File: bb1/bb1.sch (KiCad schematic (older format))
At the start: 48 parts, among them CON1 SD_Card, P1 CONN_01X02, P10 CONN_01X02, P12 CONN_01X02, P2 CONN_01X02, P3 CONN_01X02, P4 CONN_01X02, P5 CONN_01X02, P6 CONN_02X02, P7 CONN_01X02, P8 CONN_02X04, P9 CONN_02X02, Q1 MMBT3904, SW1 SW_PUSH, U1 ESP-13-WROOM-02, U2 MCP2551-I/SN, U3 WS2812RGB, U4 SN75C3222E, U5 ILI9341_LCD_Breakout, U6 WS2812RGB, U7 WS2812RGB, U8 Teensy_3.1, U9 TL2575

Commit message: v0.1 almost done now. Schematic + Board
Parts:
- removed C1, C6, C8: C_Small, Capacitors_SMD:C_1206_HandSoldering, symbol C_Small
- removed C2, C4, C5, C7: .1uF, Capacitors_SMD:C_1206_HandSoldering, symbol C_Small
- removed D1, D3: ZENERsmall, Diodes_SMD:SOD-323, symbol ZENERsmall
- removed F1: FUSE, Fuse_Holders_and_Fuses:Fuseholder5x20_horiz_SemiClosed_Casing10x25mm, symbol FUSE
- removed P1, P10, P12, P2, P3, P4, P5, P7: CONN_01X02, Terminal_Blocks:TerminalBlock_Pheonix_PT-3.5mm_2pol, symbol CONN_01X02
- removed P6, P9: CONN_02X02, Pin_Headers:Pin_Header_Straight_2x02, symbol CONN_02X02
- removed R3: 10k, Resistors_SMD:R_1206_HandSoldering, symbol R
- removed R4, R9: 68k, Resistors_SMD:R_1206_HandSoldering, symbol R
- removed SW1: SW_PUSH, Buttons_Switches_SMD:SW_SPST_FSMSM, symbol SW_PUSH
- removed U2: MCP2551-I/SN, Power_Integrations:SO-8, symbol MCP2551-I/SN
- removed U3, U6, U7: WS2812RGB, symbol WS2812RGB
- removed U4: SN75C3222E, SMD_Packages:SSOP-20, symbol SN75C3222E
- removed U8: Teensy_3.1, kicad-teensy31:Teensy-3.1, symbol Teensy_3.1
- added C24, C25, C27, C28: .1uF, Capacitors_SMD:C_0603_HandSoldering, symbol C_Small
- added E1: Encoder_switch, w_misc_comp:encoder_alps-ec12d, symbol Encoder_switch
- added P10: SPI_DBG, bb:HEADER_2x4_0.05, symbol CONN_02X04
- added P11: RX1, Measurement_Points:Measurement_Point_Round-TH_Small, symbol CONN_01X01
- added P12: RX2, Measurement_Points:Measurement_Point_Round-TH_Small, symbol CONN_01X01
- added P13: CAN_RX, Measurement_Points:Measurement_Point_Round-TH_Small, symbol CONN_01X01
- added P14: CAN_TX, Measurement_Points:Measurement_Point_Round-TH_Small, symbol CONN_01X01
- added P3: CONN_01X08, Pin_Headers:Pin_Header_Straight_1x08, symbol CONN_01X08
- added R21, R22: 4.7k, Resistors_SMD:R_0603_HandSoldering, symbol R
- added R6: 10k, Resistors_SMD:R_0603_HandSoldering, symbol R
- added R7: 56k .1%, Resistors_SMD:R_0603_HandSoldering, symbol R
- added SW3: SW_PUSH, bb:SWITCH_SMD_3x6, symbol SW_PUSH
- added U13: BMP280, bb:BMP280, symbol BMP280
- added U14: MPL3115A2, bb:MPL3115A2, symbol MPL3115A2
- added U2: WIFI_RGB, bb:WS2818RGB, symbol WS2812RGB
- added U4: N2K_RGB, bb:WS2818RGB, symbol WS2812RGB
- added U5: NMEA_RGB, bb:WS2818RGB, symbol WS2812RGB
- C1: renamed from C9; footprint Capacitors_SMD:c_elec_6.3x5.3 -> Capacitors_ThroughHole:C_Radial_D8_L11.5_P3.5
- C2: renamed from C10; footprint Capacitors_SMD:c_elec_6.3x5.3 -> Capacitors_ThroughHole:C_Radial_D6.3_L11.2_P2.5
- C3: value 0.1uF -> .1uF; footprint Capacitors_SMD:C_1206_HandSoldering -> Capacitors_SMD:C_0603_HandSoldering
- CON1: footprint 10067847-001 -> w_conn_misc:microsd_socket
- D1: renamed from D4; footprint Diodes_SMD:SOD-323 -> Diodes_SMD:SOD-123
- D2: value ZENERsmall -> 5.1V
- L1: footprint Inductors:SELF-WE-TPC_M -> bb:SRN1060_HANDSOLDER
- P2: renamed from P8; value CONN_02X04 -> WIFI_DBG; footprint Pin_Headers:Pin_Header_Straight_2x04 -> bb:HEADER_2x4_0.05
- R1: footprint Resistors_SMD:R_1206_HandSoldering -> Resistors_SMD:R_0603_HandSoldering
- R2: value 68k -> 10k; footprint Resistors_SMD:R_1206_HandSoldering -> Resistors_SMD:R_0603_HandSoldering
- R3: renamed from R5; footprint Resistors_SMD:R_1206_HandSoldering -> Resistors_SMD:R_0603_HandSoldering
- R4: renamed from R6; footprint Resistors_SMD:R_1206_HandSoldering -> Resistors_SMD:R_0603_HandSoldering
- R5: renamed from R7; footprint Resistors_SMD:R_1206_HandSoldering -> Resistors_SMD:R_0603_HandSoldering
- R8: value 10k -> 10k .1%; footprint Resistors_SMD:R_1206_HandSoldering -> Resistors_SMD:R_0603_HandSoldering
- U6: renamed from U5; footprint (none) -> bb:ILI9341
- renumbered U9 to U1, U1 to U3
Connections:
- net labels added: CAN_STBY, SCL1, SDA1, SER_EN
- net labels removed: AUX1, AUX2, CAN_RX, CAN_TX, N2K_H, N2K_L, NMEA1_RX, NMEA1_TX, NMEA2_RX, NMEA2_TX, SER1_RX, SER1_TX, SER2_RX, SER2_TX
- wire segments 215 -> 221
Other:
- moved on the sheet: C1, C2, D1, L1, Q1, R3, R4, R5, U1, U6

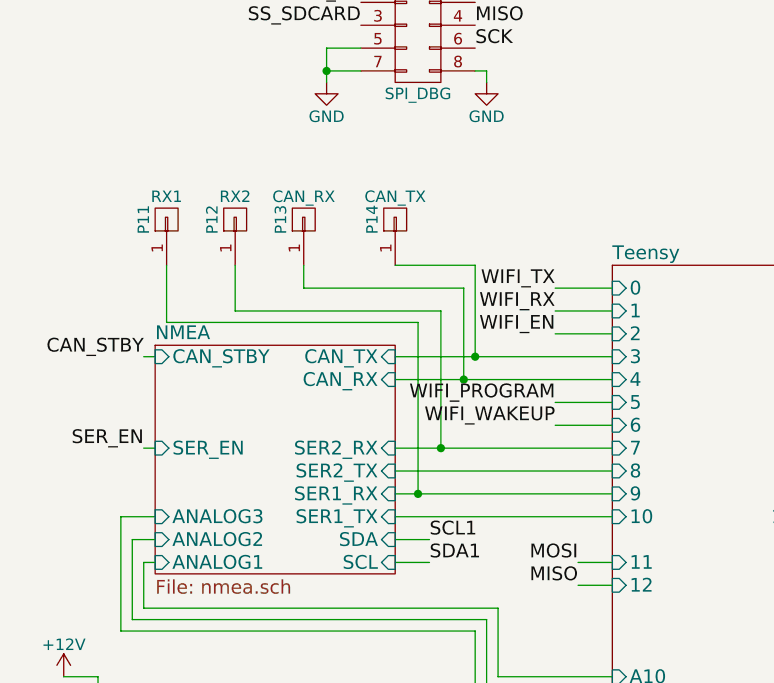
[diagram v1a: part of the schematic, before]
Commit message: Fine tuning of the board
- Added test headers for serial1, serial2 and can (at 3.3v levels)
- Added solder jumpers to disconnect serial2 from rs232 converter
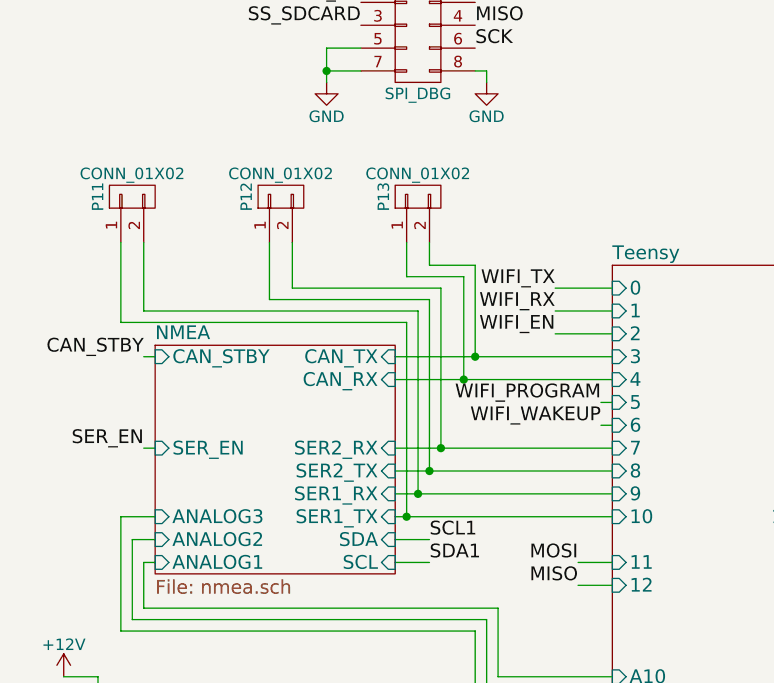
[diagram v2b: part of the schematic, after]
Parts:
- removed P11: RX1, Measurement_Points:Measurement_Point_Round-TH_Small, symbol CONN_01X01
- removed P12: RX2, Measurement_Points:Measurement_Point_Round-TH_Small, symbol CONN_01X01
- removed P13: CAN_RX, Measurement_Points:Measurement_Point_Round-TH_Small, symbol CONN_01X01
- removed P14: CAN_TX, Measurement_Points:Measurement_Point_Round-TH_Small, symbol CONN_01X01
- added P11, P12, P13: CONN_01X02, Pin_Headers:Pin_Header_Straight_1x02, symbol CONN_01X02
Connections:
- net NMEA/CAN_RX: now also P13.1 (P1)
- net NMEA/CAN_TX: now also P13.2 (P2)
- net NMEA/SER1_RX: now also P11.2 (P2)
- net NMEA/SER1_TX: now also P11.1 (P1)
- net NMEA/SER2_RX: now also P12.2 (P2)
- net NMEA/SER2_TX: now also P12.1 (P1)
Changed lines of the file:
@@
 F14 "SCL" I R 2150 5700 60
 $EndSheet
-Text Label 2850 5000 2    60   ~ 0
+Text Label 3050 5000 2    60   ~ 0
 WIFI_PROGRAM
-Text Label 2850 5100 2    60   ~ 0
+Text Label 3050 5100 2    60   ~ 0
 WIFI_WAKEUP
 Text Label 2950 5700 2    60   ~ 0
@@
 	2150 4900 3100 4900
 Wire Wire Line
-	2850 5000 3100 5000
-Wire Wire Line
-	3100 5100 2850 5100
+	3050 5000 3100 5000
+Wire Wire Line
+	3100 5100 3050 5100
 Wire Wire Line
 	2150 5500 3100 5500
@@
 Wire Wire Line
 	2550 3550 2550 3600
-$Comp
-L CONN_01X01 P13
-U 1 1 56665450
-P 1750 4200
-F 0 "P13" H 1750 4300 50  0000 C CNN
-F 1 "CAN_RX" V 1850 4200 50  0000 C CNN
-F 2 "Measurement_Points:Measurement_Point_Round-TH_Small" H 1750 4200 60  0001 C CNN
-F 3 "" H 1750 4200 60  0000 C CNN
-	1    1750 4200
-	0    -1   -1   0
-$EndComp
-$Comp
-L CONN_01X01 P14
-U 1 1 56666F3A
-P 2150 4200
-F 0 "P14" H 2150 4300 50  0000 C CNN
-F 1 "CAN_TX" V 2250 4200 50  0000 C CNN
-F 2 "Measurement_Points:Measurement_Point_Round-TH_Small" H 2150 4200 60  0001 C CNN
-F 3 "" H 2150 4200 60  0000 C CNN
-	1    2150 4200
-	0    -1   -1   0
-$EndComp
-Wire Wire Line
-	2500 4800 2500 4400
-Wire Wire Line
-	2500 4400 2150 4400
+Wire Wire Line
+	2500 4400 2500 4800
 Connection ~ 2500 4800
 Wire Wire Line
-	2450 4900 2450 4500
-Wire Wire Line
-	2450 4500 1750 4500
-Wire Wire Line
-	1750 4500 1750 4400
+	2450 4900 2450 4450
+Wire Wire Line
+	2450 4450 2200 4450
+Wire Wire Line
+	2200 4450 2200 4300
 Connection ~ 2450 4900
-$Comp
-L CONN_01X01 P12
-U 1 1 56675FE9
-P 1450 4200
-F 0 "P12" H 1450 4300 50  0000 C CNN
-F 1 "RX2" V 1550 4200 50  0000 C CNN
-F 2 "Measurement_Points:Measurement_Point_Round-TH_Small" H 1450 4200 60  0001 C CNN
-F 3 "" H 1450 4200 60  0000 C CNN
-	1    1450 4200
-	0    -1   -1   0
-$EndComp
-$Comp
-L CONN_01X01 P11
-U 1 1 566761A9
-P 1150 4200
-F 0 "P11" H 1150 4300 50  0000 C CNN
-F 1 "RX1" V 1250 4200 50  0000 C CNN
-F 2 "Measurement_Points:Measurement_Point_Round-TH_Small" H 1150 4200 60  0001 C CNN
-F 3 "" H 1150 4200 60  0000 C CNN
-	1    1150 4200
-	0    -1   -1   0
-$EndComp
-Wire Wire Line
-	1450 4400 1450 4600
-Wire Wire Line
-	1450 4600 2350 4600
-Wire Wire Line
-	2350 4600 2350 5200
+Wire Wire Line
+	1700 4300 1700 4500
+Wire Wire Line
+	1700 4500 2350 4500
+Wire Wire Line
+	2350 4500 2350 5200
 Connection ~ 2350 5200
 Wire Wire Line
-	1150 4400 1150 4650
-Wire Wire Line
-	1150 4650 2250 4650
-Wire Wire Line
-	2250 4650 2250 5400
+	1050 4300 1050 4600
+Wire Wire Line
+	1050 4600 2250 4600
+Wire Wire Line
+	2250 4600 2250 5400
 Connection ~ 2250 5400
 Wire Wire Line
@@
 SDA1
 NoConn ~ 3100 6500
+Wire Wire Line
+	1600 4300 1600 4550
+Wire Wire Line
+	1600 4550 2300 4550
+Wire Wire Line
+	2300 4550 2300 5300
+Connection ~ 2300 5300
+Wire Wire Line
+	2200 5500 2200 4650
+Wire Wire Line
+	2200 4650 950  4650
+Wire Wire Line
+	950  4650 950  4300
+Connection ~ 2200 5500
+$Comp
+L CONN_01X02 P11
+U 1 1 56608870
+P 1000 4100
+F 0 "P11" H 1000 4250 50  0000 C CNN
+F 1 "CONN_01X02" V 1100 4100 50  0000 C CNN
+F 2 "Pin_Headers:Pin_Header_Straight_1x02" H 1000 4100 60  0001 C CNN
+F 3 "" H 1000 4100 60  0000 C CNN
+	1    1000 4100
+	0    -1   -1   0
+$EndComp
+$Comp
+L CONN_01X02 P12
+U 1 1 56608D47
+P 1650 4100
+F 0 "P12" H 1650 4250 50  0000 C CNN
+F 1 "CONN_01X02" V 1750 4100 50  0000 C CNN
+F 2 "Pin_Headers:Pin_Header_Straight_1x02" H 1650 4100 60  0001 C CNN
+F 3 "" H 1650 4100 60  0000 C CNN
+	1    1650 4100
+	0    -1   -1   0
+$EndComp
+$Comp
+L CONN_01X02 P13
+U 1 1 5660A2E6
+P 2250 4100
+F 0 "P13" H 2250 4250 50  0000 C CNN
+F 1 "CONN_01X02" V 2350 4100 50  0000 C CNN
+F 2 "Pin_Headers:Pin_Header_Straight_1x02" H 2250 4100 60  0001 C CNN
+F 3 "" H 2250 4100 60  0000 C CNN
+	1    2250 4100
+	0    -1   -1   0
+$EndComp
+Wire Wire Line
+	2500 4400 2300 4400
+Wire Wire Line
+	2300 4400 2300 4300
 $EndSCHEMATC

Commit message: Continued work on the PCB. Lots of footprint work.
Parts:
- removed CON1: SD_Card, w_conn_misc:microsd_socket, symbol SD_Card
- added CON1: MICROSD, bb:DM3CS-SF, symbol MICROSD
- U1: value TL2575 -> U1
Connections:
- net +3V3: now also P3.8 (P8), CON1.4 (Vdd); no longer P3.1 (P1)
- net GND: now also P3.1 (P1), CON1.6 (VSS); no longer P3.8 (P8)
- net MISO: now also CON1.7 (DAT0/DO)
- net MOSI: now also CON1.3 (CMD/DI)
- net SCK: now also CON1.5 (CLK/SCLK)
- net SS_SDCARD: now also CON1.2 (DAT3/CS)

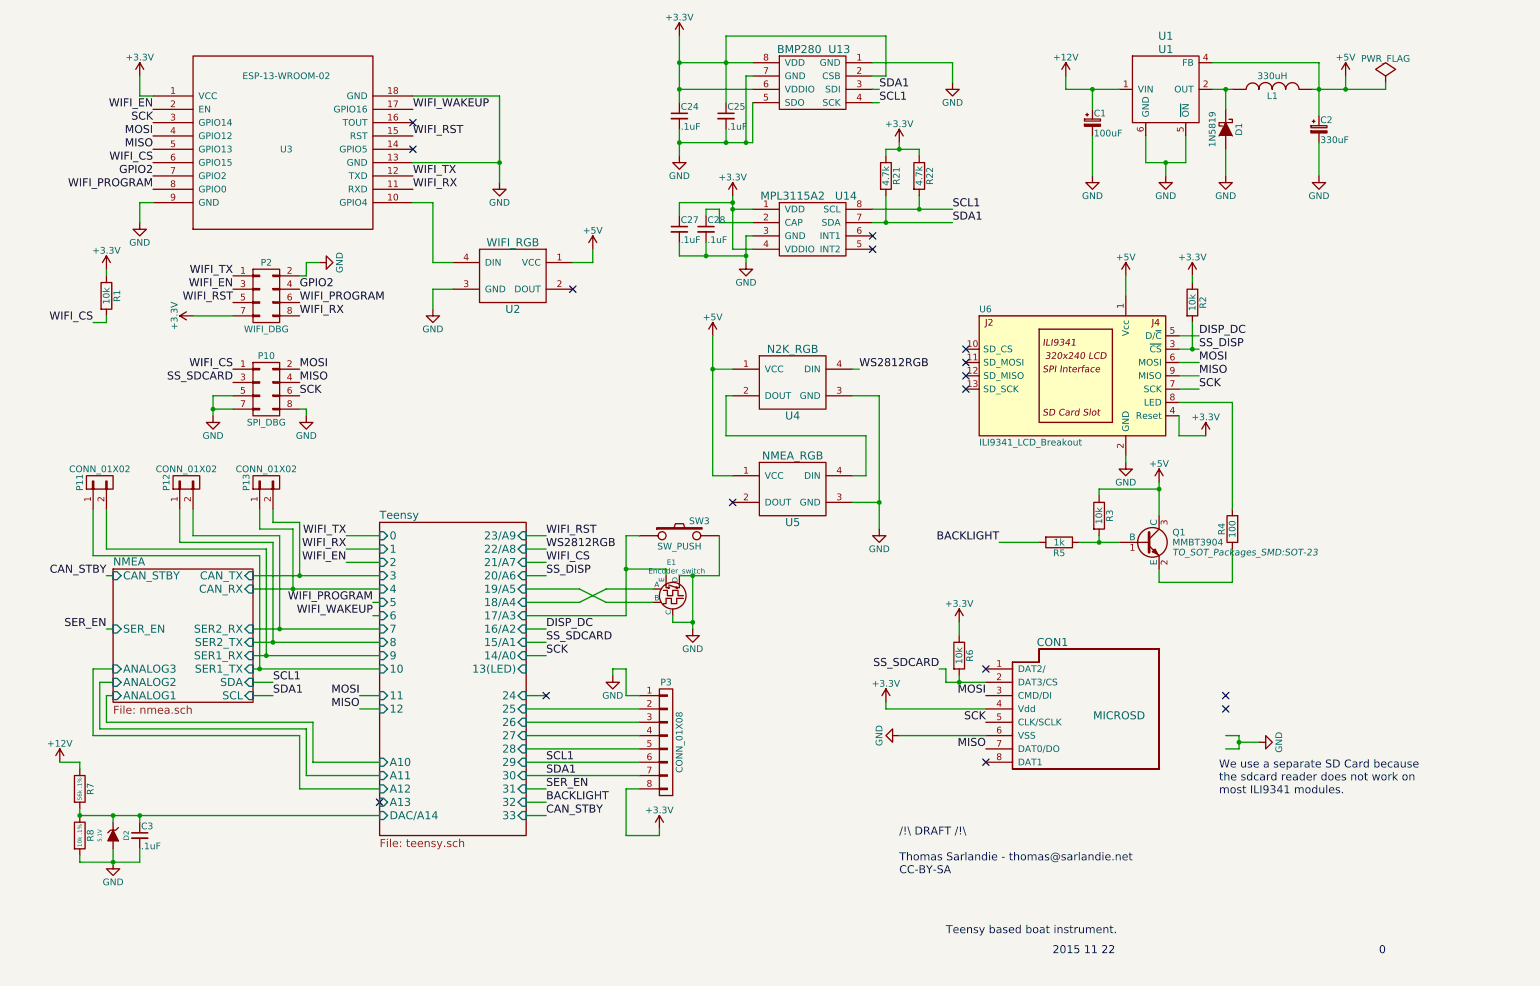
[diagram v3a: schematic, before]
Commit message: Finalized v1 revA
 - Added BNO055
 - Fixed SOIC8 pattern
 - Replaced phoenix connectors by a 20 pol
 - Many fine tuning/cosmetic adjustments
 - Sent files to manufacturing. Will tag this commit.
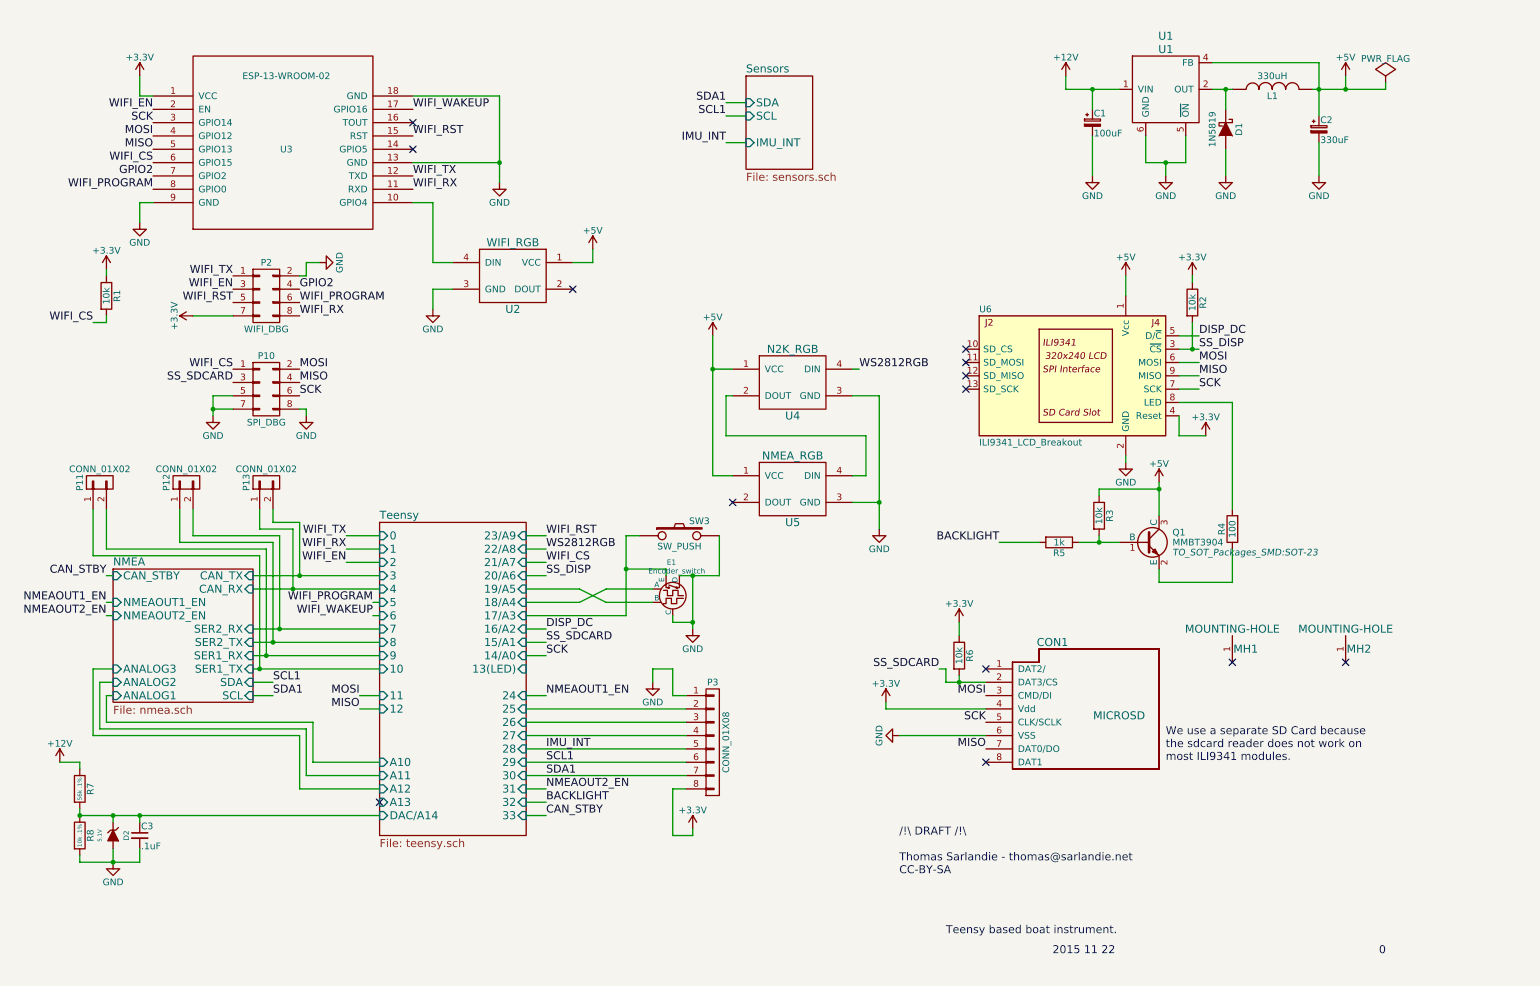
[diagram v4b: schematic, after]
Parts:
- removed C24, C25, C27, C28: .1uF, Capacitors_SMD:C_0603_HandSoldering, symbol C_Small
- removed R21, R22: 4.7k, Resistors_SMD:R_0603_HandSoldering, symbol R
- removed U13: BMP280, bb:BMP280, symbol BMP280
- removed U14: MPL3115A2, bb:MPL3115A2, symbol MPL3115A2
- added MH1, MH2: MOUNTING-HOLE, Mounting_Holes:MountingHole_4-5mm, symbol MOUNTING-HOLE
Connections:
- net Teensy/28 renamed IMU_INT
- no-connect marks 16 -> 13
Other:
- moved on the sheet: P3
